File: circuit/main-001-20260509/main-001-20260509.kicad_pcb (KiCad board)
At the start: 2 copper layers, 43.3 x 63 mm, 20 parts, among them J1 Conn_Relay, J2 Conn_Sub, Q1 BSS138, Q2 BSS138, SW1 RESET, U1 DEV-16771, U2 BNO055

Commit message: Update メイン基板のPCB完成
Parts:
- J1: value Conn_Relay -> Conn_02x09_Odd_Even; footprint Connector_PinSocket_2.54mm:PinSocket_2x08_P2.54mm_Vertical -> Connector_PinHeader_2.54mm:PinHeader_2x09_P2.54mm_Vertical
- moved R9 106.5 mm to (207.0, 48.0), turned to 90 degrees
- moved D1 105.3 mm to (204.0, 48.0), turned to 90 degrees
- moved C2 81.9 mm to (212.0, 51.6), turned to 90 degrees
- moved SW1 81.1 mm to (211.1, 51.6), turned to 90 degrees
- moved R8 80.2 mm to (210.0, 51.6), turned to -90 degrees
- moved J1 78.5 mm to (176.5, 71.3)
- moved BZ1 76.0 mm to (188.9, 50.3)
- moved C1 76.0 mm to (188.9, 70.9)
- moved J2 76.0 mm to (175.2, 61.1)
- moved Q1 76.0 mm to (175.2, 59.1)
- moved Q2 76.0 mm to (175.2, 63.1)
- moved R1 76.0 mm to (175.2, 56.1)
- moved R2 76.0 mm to (175.2, 68.1)
- moved R3 76.0 mm to (175.2, 54.1)
- moved R4 76.0 mm to (175.2, 66.1)
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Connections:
- J1 pad 1: +3.3V -> Motor_{EN}
- J1 pad 10: Dribbler_{Front-PWM} -> +3.3V
- J1 pad 11: Dribbler_{Front-EN} -> BallCatch_{Front}
- J1 pad 12: BallCatch_{Front} -> +5V
- J1 pad 13: BallCatch_{Back} -> GND
- J1 pad 14: Kicker_{Stroke} -> BallCatch_{Back}
- J1 pad 15: EN_{BOOST} -> Dribbler_{Back}
- J1 pad 2: Motor1_{PWM} -> TX_{teensy}-RX_{Arduino}-5V
- J1 pad 3: Motor2_{PWM} -> Motor1_{PWM}
- J1 pad 4: Motor3_{PWM} -> RX_{teensy}-TX_{Arduino}-5V
- J1 pad 5: Motor4_{PWM} -> Motor2_{PWM}
- J1 pad 6: Motor_{EN} -> Dribbler_{Front-PWM}
- J1 pad 7: RX_{teensy}-TX_{Arduino}-5V -> Motor3_{PWM}
- J1 pad 8: TX_{teensy}-RX_{Arduino}-5V -> Dribbler_{Front-EN}
- J1 pad 9: Dribbler_{Back} -> Motor4_{PWM}
- J2 pad 1: +3.3V -> RX_{teensy}-TX_{unitV2}
- J2 pad 10: RX_{teensy}-TX_{unitV3} -> +3.3V
- J2 pad 11: TX_{teensy}-RX_{unitV4} -> +5V
- J2 pad 12: RX_{teensy}-TX_{unitV4} -> GND
- J2 pad 13: TX_{teensy}-RX_{unitV5} -> RX_{teensy}-TX_{ESP32C301}
- J2 pad 14: RX_{teensy}-TX_{unitV5} -> TX_{teensy}-RX_{ESP32C301}
- J2 pad 15: TX_{teensy}-RX_{ESP32C302} -> RX_{teensy}-TX_{unitV3}
- J2 pad 16: RX_{teensy}-TX_{ESP32C302} -> TX_{teensy}-RX_{unitV3}
- J2 pad 17: RX_{teensy}-TX_{ESP32C301} -> TX_{teensy}-RX_{unitV4}
- J2 pad 18: TX_{teensy}-RX_{ESP32C301} -> RX_{teensy}-TX_{unitV4}
- J2 pad 2: GND -> TX_{teensy}-RX_{unitV2}
- J2 pad 3: GND -> SW_{START}
- J2 pad 4: SW_{START} -> TX_{teensy}-RX_{unitV1}
- J2 pad 5: TX_{teensy}-RX_{unitV1} -> RX_{teensy}-TX_{unitV1}
- J2 pad 6: RX_{teensy}-TX_{unitV1} -> RX_{teensy}-TX_{ESP32C302}
- J2 pad 7: TX_{teensy}-RX_{unitV2} -> TX_{teensy}-RX_{ESP32C302}
- J2 pad 8: RX_{teensy}-TX_{unitV2} -> TX_{teensy}-RX_{unitV5}
- J2 pad 9: TX_{teensy}-RX_{unitV3} -> RX_{teensy}-TX_{unitV5}
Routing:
- net +5V: track 0.00 -> 98.4 mm, vias 0 -> 3
- net +3.3V: track 33.1 -> 114.7 mm, vias 1 -> 6
- net RX_{teensy}-TX_{unitV5}: track 0.00 -> 59.3 mm
- net Main_RST: track 0.00 -> 58.3 mm
- net TX_{teensy}-RX_{unitV5}: track 0.00 -> 56.4 mm
- net LED: track 7.62 -> 60.2 mm, vias 0 -> 2
- net Dribbler_{Front-EN}: track 0.00 -> 39.9 mm
- net Dribbler_{Front-PWM}: track 0.00 -> 38.9 mm
- net GND: track 0.00 -> 37.5 mm, vias 0 -> 1
- net TX_{teensy}-RX_{unitV4}: track 0.00 -> 36.6 mm
- net RX_{teensy}-TX_{unitV4}: track 0.00 -> 33.1 mm
- net RX_{teensy}-TX_{unitV3}: track 0.00 -> 31.0 mm
- net TX_{teensy}-RX_{ESP32C302}: track 0.00 -> 29.4 mm
- net RX_{teensy}-TX_{ESP32C302}: track 0.00 -> 29.2 mm
- net RX_{teensy}-TX_{unitV1}: track 0.00 -> 27.0 mm
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- added copper zone on B.Cu, net GND
- added copper zone on F.Cu, net GND
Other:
- board size 43.3 x 63 mm -> 43.3 x 83.2 mm

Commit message: Update メイン基板をDRした
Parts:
- moved BZ1 145.3 mm to (44.5, 34.0)
- moved C1 145.3 mm to (44.5, 54.6)
- moved D1 145.3 mm to (59.6, 31.7)
- moved J1 145.3 mm to (32.1, 55.0)
- moved R5 145.3 mm to (44.5, 49.5)
- moved R6 145.3 mm to (44.5, 34.0)
- moved R7 145.3 mm to (44.5, 47.0)
- moved R9 145.3 mm to (62.6, 31.7)
- moved SW1 145.3 mm to (66.7, 35.3)
- moved U1 145.3 mm to (44.5, 58.4)
- moved U2 145.3 mm to (44.5, 50.8)
- moved J2 145.3 mm to (30.8, 44.9)
- moved Q1 145.3 mm to (30.8, 42.9)
- moved Q2 145.3 mm to (30.8, 46.9)
- moved R1 145.3 mm to (30.8, 39.9)
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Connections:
- J2 pad 1: RX_{teensy}-TX_{unitV2} -> TX_{teensy}-RX_{unitV2}
- J2 pad 2: TX_{teensy}-RX_{unitV2} -> RX_{teensy}-TX_{unitV2}
- J2 pad 3: SW_{START} -> TX_{teensy}-RX_{unitV1}
- J2 pad 4: TX_{teensy}-RX_{unitV1} -> RX_{teensy}-TX_{unitV1}
- J2 pad 5: RX_{teensy}-TX_{unitV1} -> RX_{teensy}-TX_{ESP32C302}
- J2 pad 6: RX_{teensy}-TX_{ESP32C302} -> TX_{teensy}-RX_{ESP32C302}
- J2 pad 7: TX_{teensy}-RX_{ESP32C302} -> TX_{teensy}-RX_{unitV5}
- J2 pad 8: TX_{teensy}-RX_{unitV5} -> SW_{START}
- U1 pad 3: SW_{START} -> unconnected-(U1-LRCLK2-Pad3)
- U1 pad 5: unconnected-(U1-IN2-Pad5) -> SW_{START}
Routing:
- net GND: track 37.5 -> 10.2 mm, vias 1 -> 0
- net +5V: track 98.4 -> 77.2 mm, vias 3 -> 4
- net RX_{teensy}-TX_{unitV5}: track 59.3 -> 52.9 mm, vias 0 -> 2
- net +3.3V: track 114.7 -> 108.3 mm
- net RX_{teensy}-TX_{unitV2}: track 22.3 -> 26.6 mm
- net TX_{teensy}-RX_{unitV5}: track 56.4 -> 53.4 mm, vias 0 -> 2
- net TX_{teensy}-RX_{unitV1}: track 26.7 -> 29.5 mm
- net RX_{teensy}-TX_{unitV1}: track 27.0 -> 29.0 mm
- net RX_{teensy}-TX_{ESP32C302}: track 29.2 -> 31.2 mm
- net TX_{teensy}-RX_{ESP32C302}: track 29.4 -> 31.2 mm
- net Main_RST: track 58.3 -> 56.6 mm
- net SW_{START}: track 5.06 -> 3.63 mm
- net Dribbler_{Back}: track 26.4 -> 25.1 mm, vias 0 -> 1
- net TX_{teensy}-RX_{unitV2}: track 23.6 -> 22.9 mm
- net RX_{teensy}-TX_{Arduino}-5V: track 22.3 -> 22.9 mm, vias 0 -> 1

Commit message: Update メイン基板を修正
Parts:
- moved BZ1 2.82 mm to (44.8, 31.2)
- moved R6 2.82 mm to (44.8, 31.2)
- moved C1 2.82 mm to (44.8, 51.8)
- moved D1 2.82 mm to (59.9, 28.9)
- moved J1 2.82 mm to (32.4, 52.2)
- moved J2 2.82 mm to (31.1, 42.1)
- moved Q1 2.82 mm to (31.1, 40.1)
- moved Q2 2.82 mm to (31.1, 44.1)
- moved R1 2.82 mm to (31.1, 37.1)
- moved R2 2.82 mm to (31.1, 49.1)
- moved R3 2.82 mm to (31.1, 35.1)
- moved R4 2.82 mm to (31.1, 47.1)
- moved R5 2.82 mm to (44.8, 46.7)
- moved R7 2.82 mm to (44.8, 44.2)
- moved R9 2.82 mm to (62.9, 28.9)
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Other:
- board text added: "D13"
- board text added: "Main-001"
- board text added: "RST"

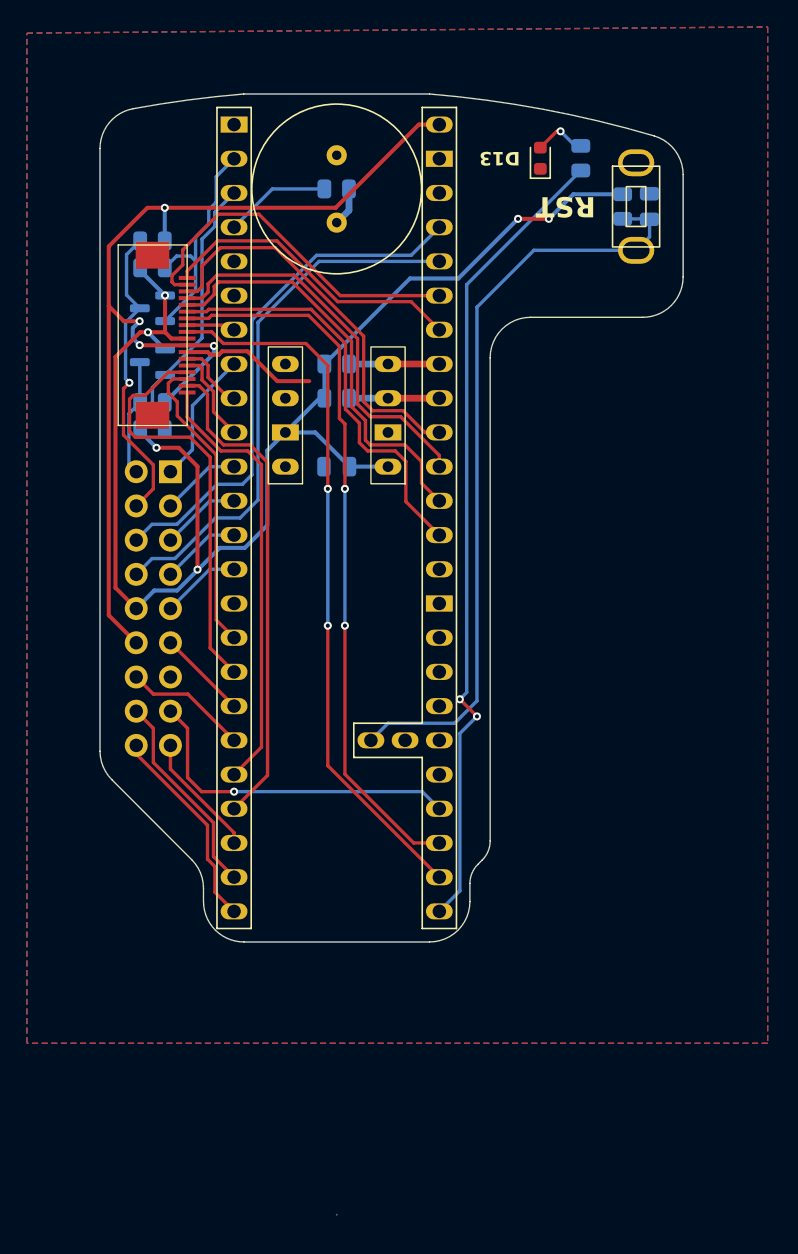
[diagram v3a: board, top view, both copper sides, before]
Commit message: Update メイン基板のBNO055のGNDに3.3Vが接続されていた問題を解決、ボード図も修正した
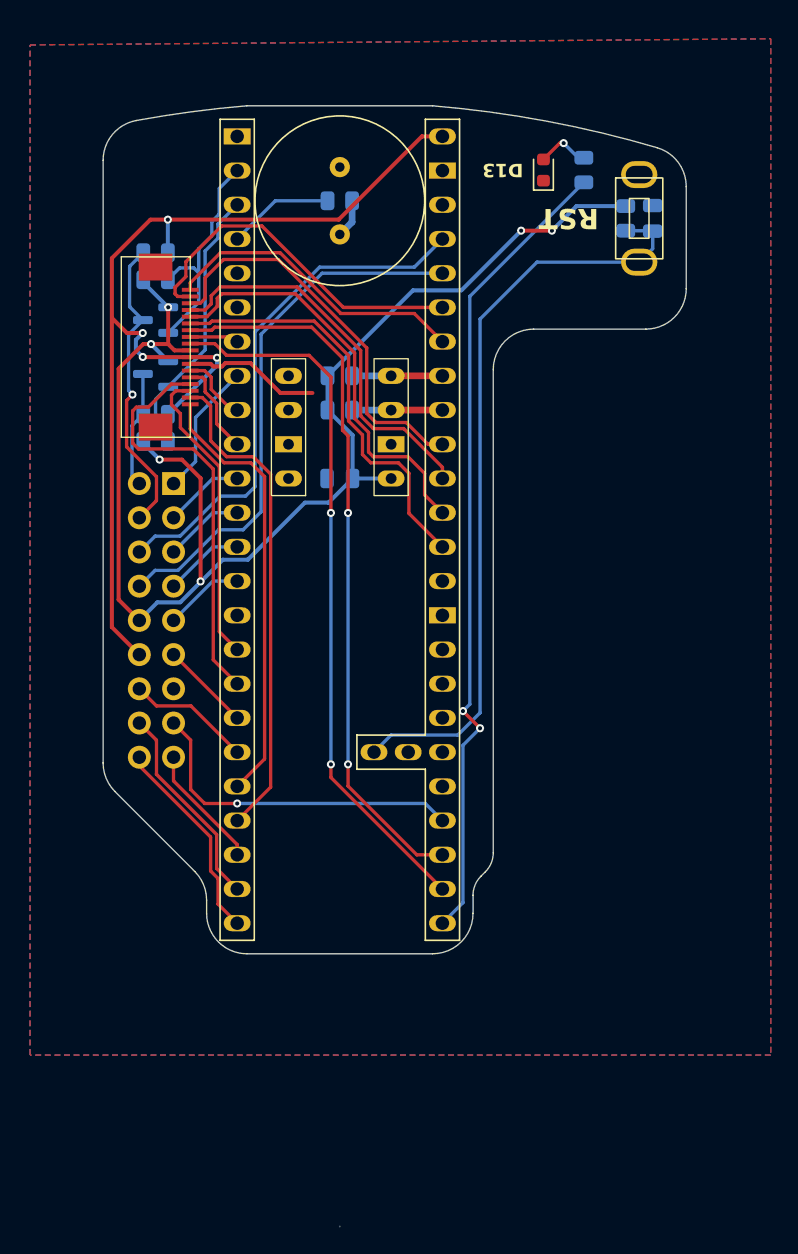
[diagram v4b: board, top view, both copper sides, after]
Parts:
- J1: value Conn_02x09_Odd_Even -> Conn_Relay
- moved J1 0.91 mm to (32.7, 53.1)
- moved U2 0.91 mm to (45.0, 48.9)
- moved BZ1 0.91 mm to (45.0, 32.1)
- moved R6 0.91 mm to (45.0, 32.1)
- moved C2 0.91 mm to (68.2, 33.4)
- moved R8 0.91 mm to (66.2, 33.4)
- moved SW1 0.91 mm to (67.2, 33.4)
- moved J2 0.91 mm to (31.3, 42.9)
- moved Q1 0.91 mm to (31.3, 40.9)
- moved Q2 0.91 mm to (31.3, 44.9)
- moved R1 0.91 mm to (31.3, 37.9)
- moved R2 0.91 mm to (31.3, 49.9)
- moved R3 0.91 mm to (31.3, 35.9)
- moved R4 0.91 mm to (31.3, 47.9)
- moved C1 0.91 mm to (45.0, 52.7)
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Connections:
- U2 pad 7: +3.3V -> GND
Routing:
- net +3.3V: track 108.3 -> 104.9 mm
